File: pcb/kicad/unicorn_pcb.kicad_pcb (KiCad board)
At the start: 2 copper layers, 100 x 85 mm, 29 parts, among them J1 Conn_01x10_Male_LEFT, J2 Conn_01x10_Male_RIGHT, SW1 SW_Push

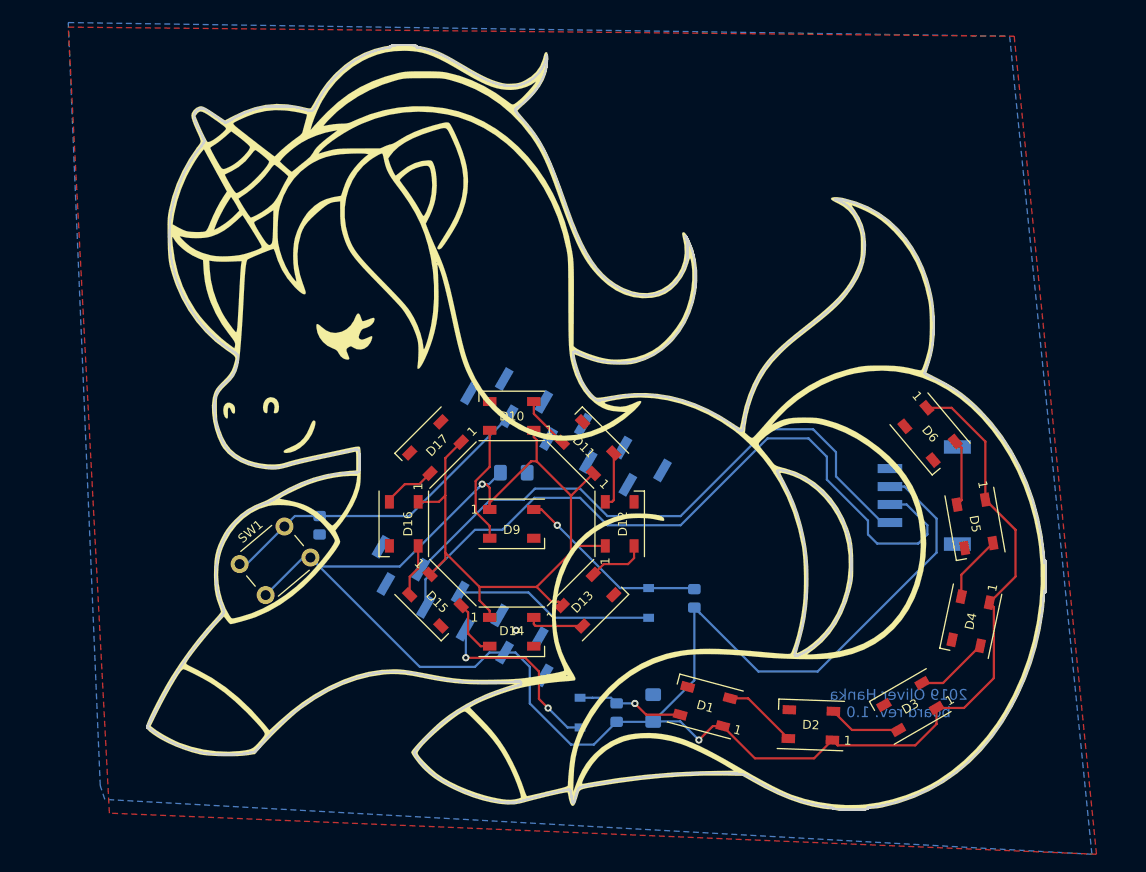
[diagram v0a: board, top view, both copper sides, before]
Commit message: pcb rev 1.1; extended board test firmware
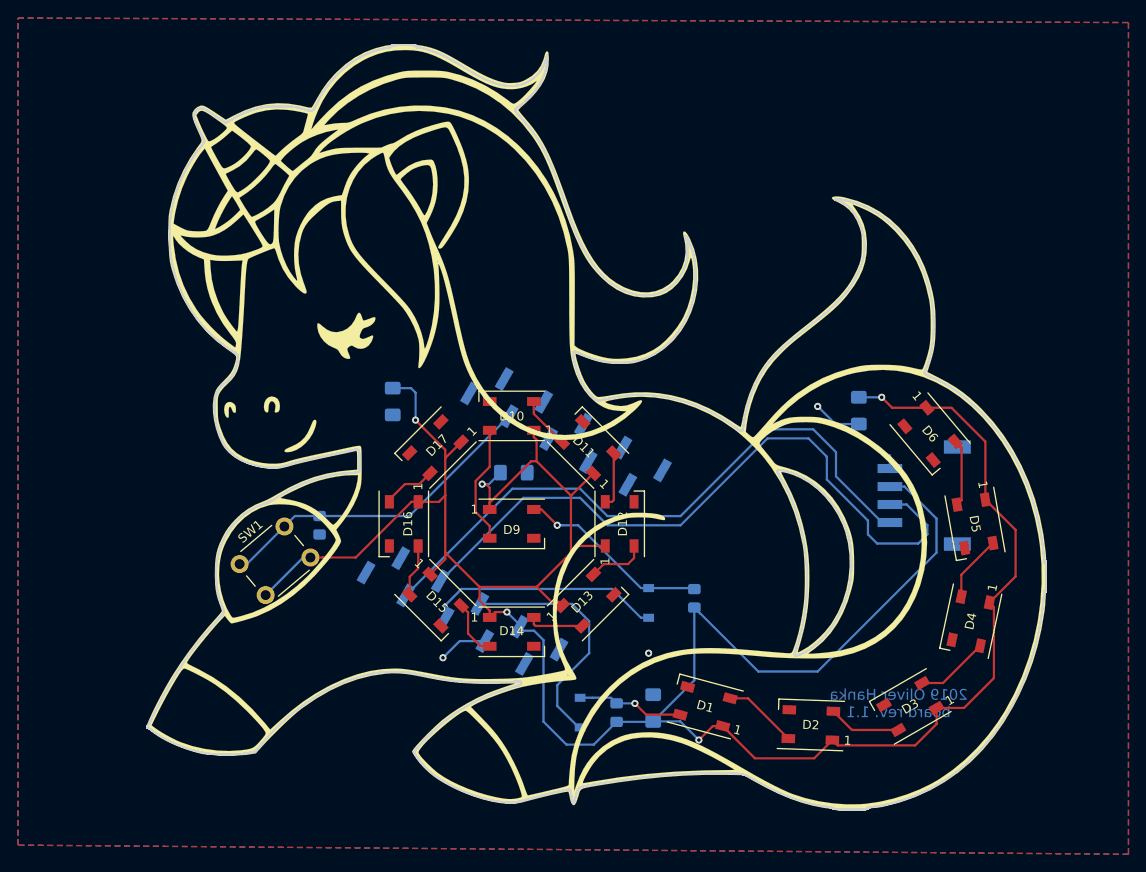
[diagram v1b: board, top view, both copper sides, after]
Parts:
- added C3: 100nF, Capacitor_SMD:C_1206_3216Metric_Pad1.42x1.75mm_HandSolder, B.Cu at (227.6, 60.4)
- added C4: 100nF, Capacitor_SMD:C_1206_3216Metric_Pad1.42x1.75mm_HandSolder, B.Cu at (175.8, 59.4)
- J2: footprint Connector_PinHeader_2.54mm:PinHeader_1x10_P2.54mm_Vertical_SMD_Pin1Left -> Connector_PinHeader_2.54mm:PinHeader_1x10_P2.54mm_Vertical_SMD_Pin1Right
- moved G*** 1.30 mm to (175.3, 39.6)
- moved REF** 0.52 mm to (232.1, 85.3)
- moved G*** 0.13 mm to (198.4, 62.1)
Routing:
- net GND: track 0.00 -> 12.3 mm, vias 1 -> 3
- net +5V: track 306.0 -> 296.2 mm, vias 2 -> 5
- net /GPIO16: track 20.9 -> 27.4 mm, vias 2 -> 0
- net /WireSDA: track 81.6 -> 77.0 mm
- net /GPIO17: track 22.1 -> 26.1 mm
- net /WireSCL: track 67.0 -> 69.9 mm
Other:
- board text added: "2019 Oliver Hanka board rev. 1.1"
- board text removed: "2019 Oliver Hanka board rev. 1.0"
